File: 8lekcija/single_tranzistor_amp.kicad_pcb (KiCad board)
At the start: 2 copper layers, 31.2 x 25.7 mm, 11 parts, among them P1 PWR_CONN, P2 SIGNAL_IN, P3 SIGNAL_OUT, Q1 BC548

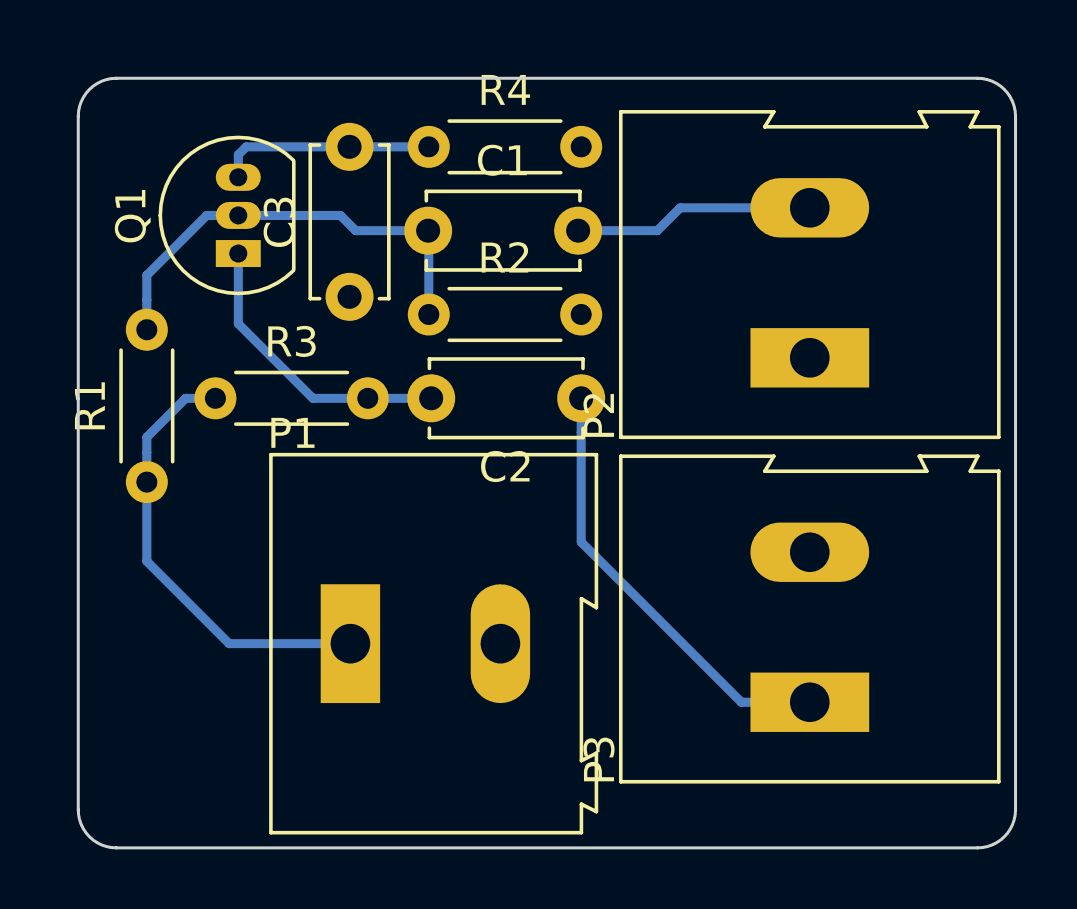
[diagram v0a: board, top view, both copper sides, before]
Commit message: Kursa darba papildinajums, lekciju darbu nobeigums
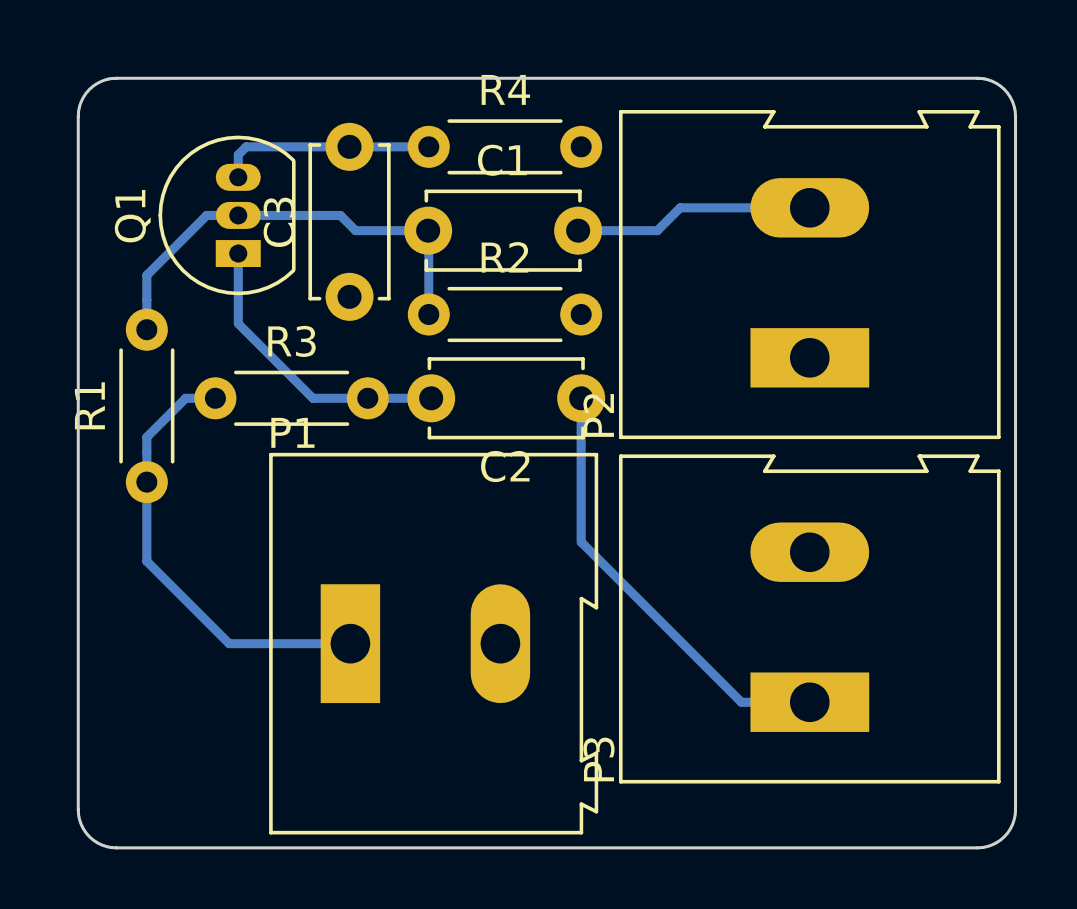
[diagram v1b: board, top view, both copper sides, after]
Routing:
- added copper zone on F.Cu, net GND
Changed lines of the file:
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@@
   (general
     (links 16)
-    (no_connects 10)
+    (no_connects 0)
     (area 164.287999 83.007999 195.630001 108.762001)
     (thickness 1.6)
@@
     (33 F.Adhes user hide)
     (35 F.Paste user hide)
-    (37 F.SilkS user hide)
+    (37 F.SilkS user)
     (39 F.Mask user hide)
     (40 Dwgs.User user hide)
@@
     (pad_to_mask_clearance 0)
     (aux_axis_origin 0 0)
-    (visible_elements 7FFFEFDF)
+    (visible_elements 7FFFE7DF)
     (pcbplotparams
-      (layerselection 0x00030_80000001)
+      (layerselection 0x00020_80000001)
       (usegerberextensions false)
       (excludeedgelayer true)
@@
       (outputformat 1)
       (mirror false)
-      (drillshape 1)
+      (drillshape 0)
       (scaleselection 1)
       (outputdirectory ""))
@@
     (polygon
       (pts
-        (xy 194.31 108.712) (xy 194.564 108.712) (xy 195.072 108.458) (xy 195.326 108.204) (xy 195.58 107.696)
-        (xy 195.58 107.442) (xy 195.58 84.074) (xy 195.326 83.566) (xy 195.072 83.312) (xy 194.564 83.058)
-        (xy 165.354 83.058) (xy 164.846 83.312) (xy 164.592 83.566) (xy 164.338 84.074) (xy 164.338 107.696)
-        (xy 164.592 108.204) (xy 164.846 108.458) (xy 165.354 108.712)
+        (xy 195.072 83.300588) (xy 195.326 83.554588) (xy 195.58 84.062588) (xy 195.58 107.696) (xy 195.326 108.204)
+        (xy 195.072 108.458) (xy 194.564 108.712) (xy 165.354 108.712) (xy 164.846 108.458) (xy 164.592 108.204)
+        (xy 164.338 107.696) (xy 164.338 84.062588) (xy 164.592 83.554588) (xy 164.846 83.300588) (xy 165.354 83.046588)
+        (xy 194.564 83.046588)
       )
     )
+  )
+  (zone (net 5) (net_name GND) (layer F.Cu) (hatch edge 0.508)
+    (connect_pads (clearance 0.508))
+    (min_thickness 0.254)
+    (fill yes (mode segment) (arc_segments 32) (thermal_gap 0.508) (thermal_bridge_width 0.508))
+    (polygon
+      (pts
+        (xy 194.31 108.698609) (xy 194.564 108.698609) (xy 195.072 108.444609) (xy 195.326 108.190609) (xy 195.58 107.682609)
+        (xy 195.58 107.428609) (xy 195.58 84.060609) (xy 195.326 83.552609) (xy 195.072 83.298609) (xy 194.564 83.044609)
+        (xy 165.354 83.044609) (xy 164.846 83.298609) (xy 164.592 83.552609) (xy 164.338 84.060609) (xy 164.338 107.682609)
+        (xy 164.592 108.190609) (xy 164.846 108.444609) (xy 165.354 108.698609)
+      )
+    )
